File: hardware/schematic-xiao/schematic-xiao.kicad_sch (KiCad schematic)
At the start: 17 parts, among them SW1 RotaryEncoder, SW2 SW_Push, SW3 SW_Push, SW4 SW_Push, SW5 SW_Push, U1 XIAO ESP32C3, U3 MCP23S17_SP

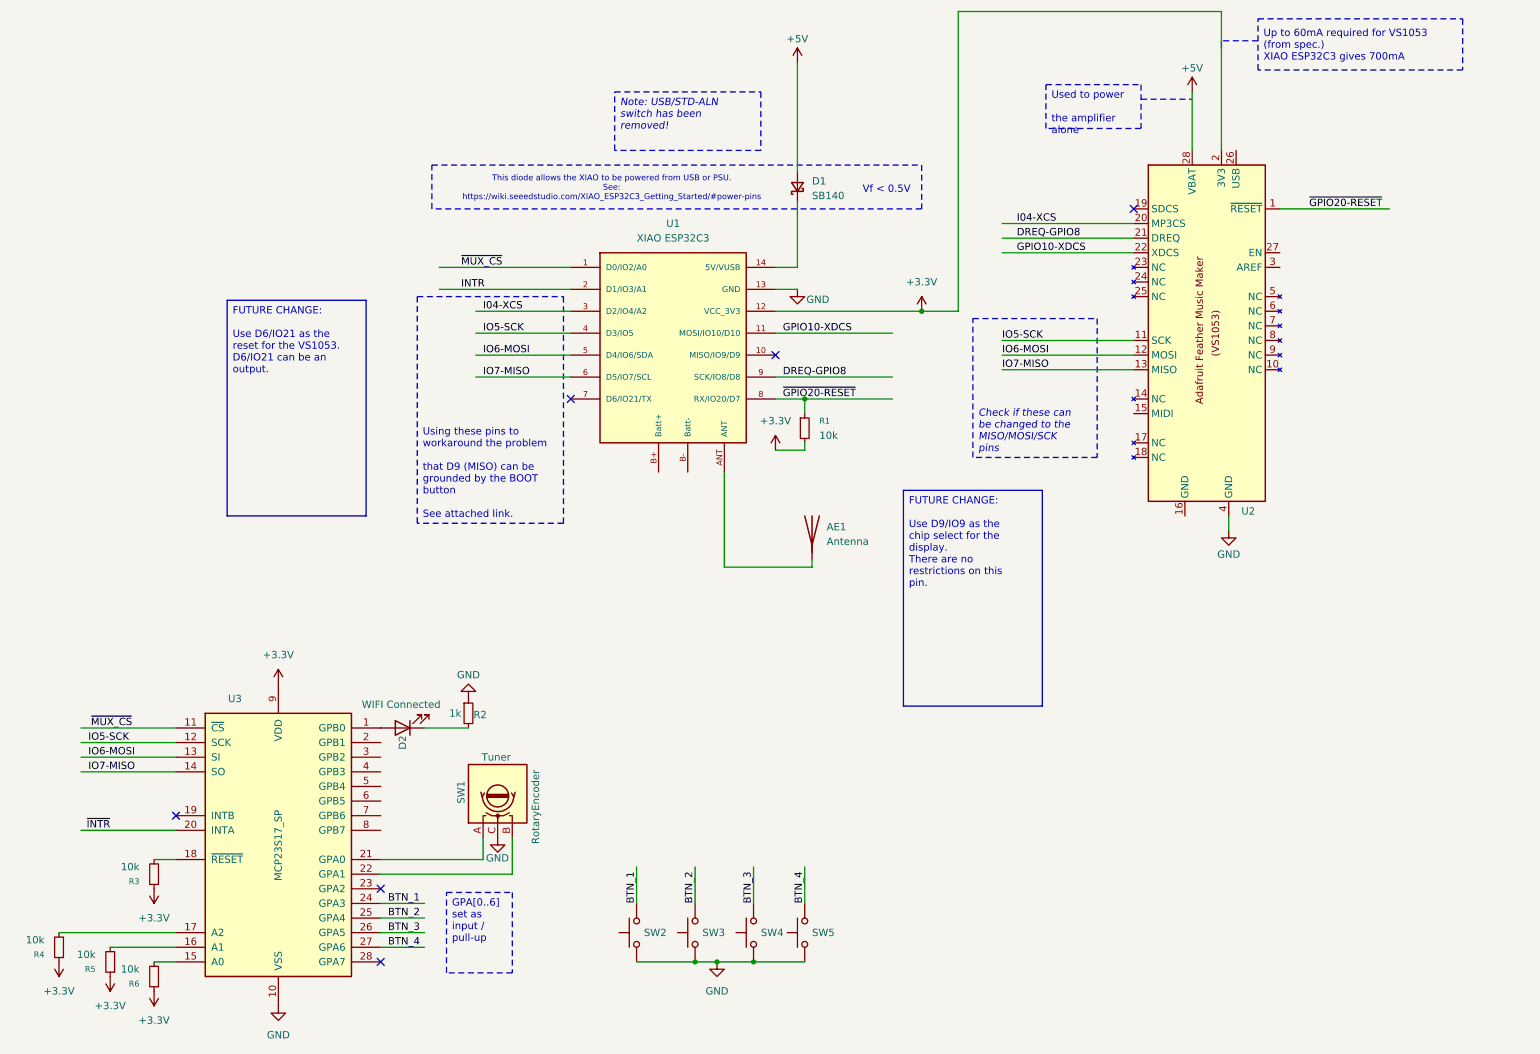
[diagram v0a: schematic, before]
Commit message: Display added to schematic + RESET_CODEC + R_SW_PU symbol
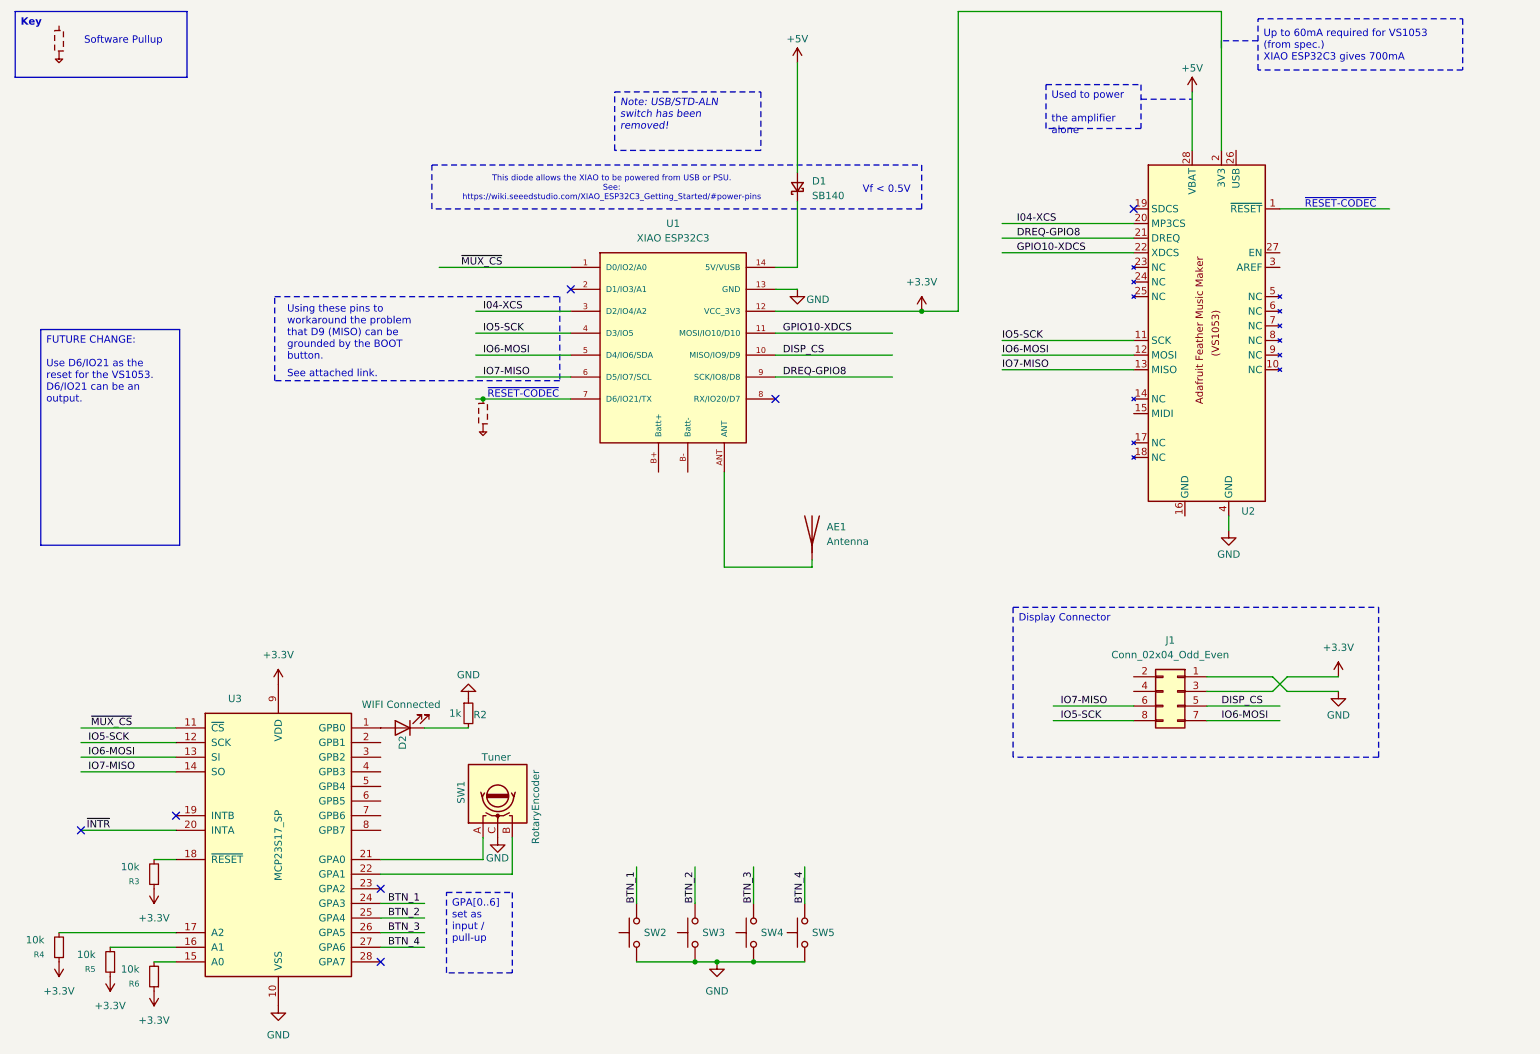
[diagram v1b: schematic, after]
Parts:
- removed R1: 10k, symbol Device:R_Small
- added J1: Conn_02x04_Odd_Even, symbol Connector_Generic:Conn_02x04_Odd_Even
- added R_SW_PU1, R_SW_PU2: ~, symbol project:R_Software_Pullup
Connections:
- net +3.3V: now also J1.3 (Pin_3)
- net GND: now also J1.1 (Pin_1)
- net IO5-SCK: now also J1.8 (Pin_8)
- net IO6-MOSI: now also J1.7 (Pin_7)
- net IO7-MISO: now also J1.6 (Pin_6)
- net DISP_CS: now reaches U1.10 (MISO/IO9/D9)
- net DISP_CS: now also J1.5 (Pin_5)
- net at U1.7 (D6/IO21/TX): now also R_SW_PU1.
- net INTR: no longer names the net of U1.2 (D1/IO3/A1)
- net ~{GPIO20-RESET}: no longer names the net of U2.1 (~{RESET})
- net ~{GPIO20-RESET}: no longer U1.8 (RX/IO20/D7)
- no-connect marks 6 -> 7
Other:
- note added: "See attached link."
- note added: "Software Pullup"
- note added: "Using these pins to workaround the problem that D9 (MISO) can be grounded by the BOOT button."
- note added: "~{RESET-CODEC}"

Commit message: Rejected using 5V for display + comments
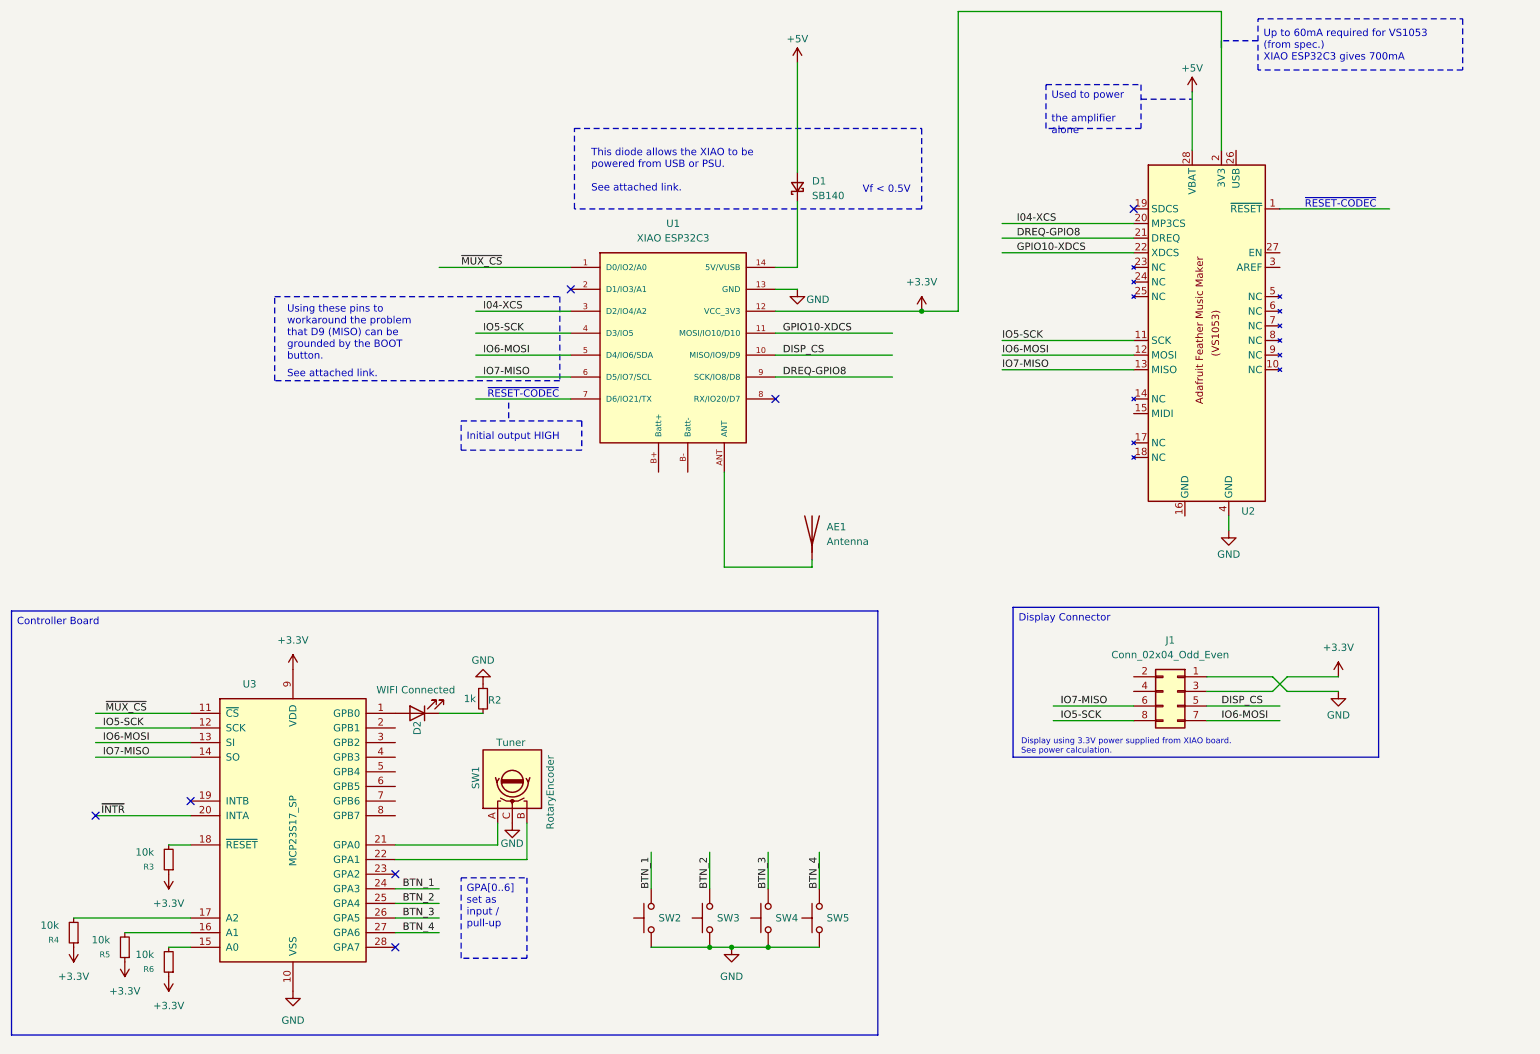
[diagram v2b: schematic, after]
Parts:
- removed R_SW_PU1, R_SW_PU2: ~, symbol project:R_Software_Pullup
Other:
- note added: "Display using 3.3V power supplied from XIAO board. See power calculation."
- note added: "This diode allows the XIAO to be powered from USB or PSU. See attached link."
- note removed: "Software Pullup"
- note removed: "This diode allows the XIAO to be powered from USB or PSU. See: https://wiki.seeedstudio.com/XIAO_ESP32C3_Getting_Started/#power-pins"
- moved on the sheet: D2, R2, R3, R4, R5, R6, SW1, SW2, SW3, SW4, SW5, U3

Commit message: Added display SPI isolator
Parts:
- added J2: Conn_01x02, symbol Connector_Generic:Conn_01x02
- added R1: 10k, symbol Device:R_Small
- added U4: 74HC244, symbol 74xx:74HC244
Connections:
- net +3.3V: now also R1.2, U4.20 (VCC); no longer J1.3 (Pin_3)
- net +5V: now also J1.3 (Pin_3), J2.1 (Pin_1)
- net DISP_CS: now also U4.1 (1OE)
- net GND: now also J2.2 (Pin_2), U4.10 (GND), U4.8 (1A3)
- net IO5-SCK: now also U4.4 (1A1); no longer J1.8 (Pin_8)
- net IO6-MOSI: now also U4.2 (1A0); no longer J1.7 (Pin_7)
- net IO7-MISO: now also U4.14 (1Y2); no longer J1.6 (Pin_6)
- new net: R1.1, U4.19 (2OE)
- new net MISO-DSIDE: J1.6 (Pin_6), U4.6 (1A2)
- new net MOSI-DSIDE: J1.7 (Pin_7), U4.18 (1Y0)
- new net SCK-DSIDE: J1.8 (Pin_8), U4.16 (1Y1)
- no-connect marks 7 -> 19
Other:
- note added: "!"
- note added: "Display board needs to be configured to use 5V as power."
- note removed: "Display using 3.3V power supplied from XIAO board. See power calculation."
- moved on the sheet: AE1, J1, SW2, SW3, SW4, SW5
